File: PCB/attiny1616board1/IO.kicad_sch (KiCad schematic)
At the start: 41 parts, among them J10 SENSOR3_IN, J11 WS2813_OUT, J12 SERVO_OUT, J13 UPDI, J14 SERIAL, J15 SOLENOID1, J16 SOLENOID2, J8 SENSOR1_IN, J9 SENSOR2_IN, Q1 S8050, Q2 S8550, Q3 AO3400A, Q4 S8050, Q5 S8550, Q6 AO3400A, SW1 SENSOR1_TEST, SW2 SENSOR2_TEST, SW3 SENSOR3_TEST, SW4 SW_DIP_x08

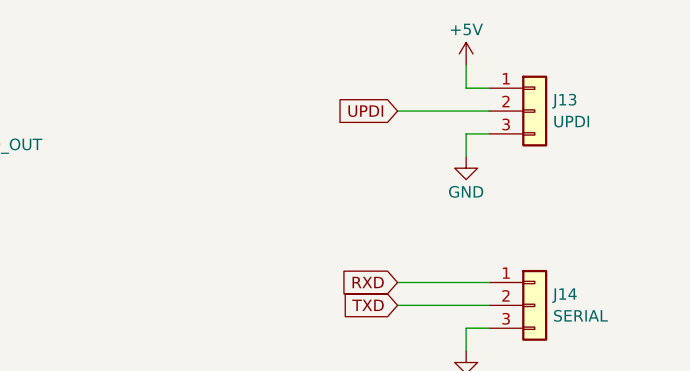
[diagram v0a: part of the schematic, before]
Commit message: 新7セグ・タイマー制御基板のデータを追加
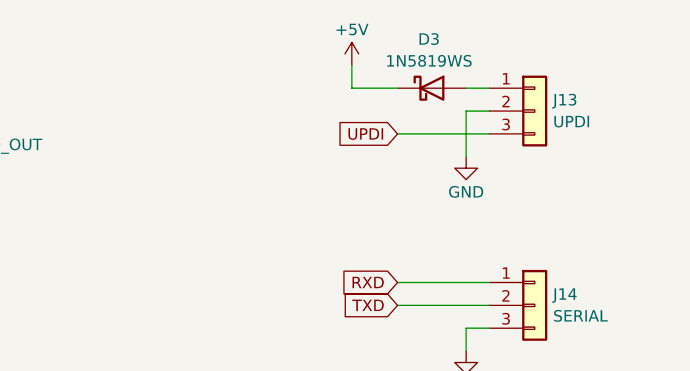
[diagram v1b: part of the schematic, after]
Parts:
- added D3: 1N5819WS, Diode_SMD:D_SOD-323, symbol Device:D_Schottky
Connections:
- net +5V: now also D3.1 (K); no longer J13.1 (Pin_1)
- net GND: now also J13.2 (Pin_2); no longer J13.3 (Pin_3)
- net UPDI: now also J13.3 (Pin_3); no longer J13.2 (Pin_2)
- new net: D3.2 (A), J13.1 (Pin_1)
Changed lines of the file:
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@@
     (stroke (width 0) (type default))
   )
-  (wire (pts (xy 251.46 30.48) (xy 251.46 33.02))
+  (wire (pts (xy 251.46 27.94) (xy 251.46 33.02))
     (stroke (width 0) (type default))
   )
@@
     (stroke (width 0) (type default))
   )
+  (wire (pts (xy 243.84 30.48) (xy 254 30.48))
+    (stroke (width 0) (type default))
+  )
   (wire (pts (xy 162.56 102.87) (xy 165.1 102.87))
     (stroke (width 0) (type default))
@@
     (stroke (width 0) (type default))
   )
-  (wire (pts (xy 254 30.48) (xy 251.46 30.48))
+  (wire (pts (xy 254 27.94) (xy 251.46 27.94))
     (stroke (width 0) (type default))
   )
@@
     (stroke (width 0) (type default))
   )
+  (wire (pts (xy 238.76 25.4) (xy 243.84 25.4))
+    (stroke (width 0) (type default))
+  )
   (wire (pts (xy 100.33 166.37) (xy 85.09 166.37))
     (stroke (width 0) (type default))
@@
     (stroke (width 0) (type default))
   )
-  (wire (pts (xy 251.46 25.4) (xy 251.46 22.86))
+  (wire (pts (xy 238.76 25.4) (xy 238.76 22.86))
     (stroke (width 0) (type default))
   )
@@
   )
   (wire (pts (xy 74.93 172.72) (xy 77.47 172.72))
-    (stroke (width 0) (type default))
-  )
-  (wire (pts (xy 243.84 27.94) (xy 254 27.94))
     (stroke (width 0) (type default))
   )
@@
     )
   )
-  (global_label "UPDI" (shape input) (at 243.84 27.94 180) (fields_autoplaced)
+  (global_label "UPDI" (shape input) (at 243.84 30.48 180) (fields_autoplaced)
     (effects (font (size 1.27 1.27)) (justify right))
-    (property "Intersheetrefs" "${INTERSHEET_REFS}" (at 236.3795 27.94 0)
+    (property "Intersheetrefs" "${INTERSHEET_REFS}" (at 236.3795 30.48 0)
       (effects (font (size 1.27 1.27)) (justify right) hide)
     )
@@
     )
   )
+  (symbol (lib_id "Device:D_Schottky") (at 247.65 25.4 0) (unit 1)
+    (in_bom yes) (on_board yes) (dnp no)
+    (property "Reference" "D3" (at 247.3325 19.9857 0)
+      (effects (font (size 1.27 1.27)))
+    )
+    (property "Value" "1N5819WS" (at 247.3325 22.4099 0)
+      (effects (font (size 1.27 1.27)))
+    )
+    (property "Footprint" "Diode_SMD:D_SOD-323" (at 247.65 25.4 0)
+      (effects (font (size 1.27 1.27)) hide)
+    )
+    (property "Datasheet" "~" (at 247.65 25.4 0)
+      (effects (font (size 1.27 1.27)) hide)
+    )
+    (property "LCSC" "C191023" (at 247.65 25.4 0)
+      (effects (font (size 1.27 1.27)) hide)
+    )
+    (pin "2")
+    (pin "1")
+    (instances
+      (project "attiny1616board1"
+        (path "/96ba6829-8a3e-4d81-9a4b-1c1c29c6350f/7613d6ae-36c0-4a05-b2dd-82f4e8851848"
+          (reference "D3") (unit 1)
+        )
+      )
+    )
+  )
   (symbol (lib_id "power:GND") (at 110.49 50.8 0) (unit 1)
     (in_bom yes) (on_board yes) (dnp no) (fields_autoplaced)
@@
     )
   )
-  (symbol (lib_id "power:+5V") (at 251.46 22.86 0) (unit 1)
-    (in_bom yes) (on_board yes) (dnp no)
-    (property "Reference" "#PWR031" (at 251.46 26.67 0)
-      (effects (font (size 1.27 1.27)) hide)
-    )
-    (property "Value" "+5V" (at 251.46 18.915 0)
-      (effects (font (size 1.27 1.27)))
-    )
-    (property "Footprint" "" (at 251.46 22.86 0)
-      (effects (font (size 1.27 1.27)) hide)
-    )
-    (property "Datasheet" "" (at 251.46 22.86 0)
-      (effects (font (size 1.27 1.27)) hide)
-    )
+  (symbol (lib_id "power:+5V") (at 238.76 22.86 0) (unit 1)
+    (in_bom yes) (on_board yes) (dnp no)
+    (property "Reference" "#PWR031" (at 238.76 26.67 0)
+      (effects (font (size 1.27 1.27)) hide)
+    )
+    (property "Value" "+5V" (at 238.76 18.915 0)
+      (effects (font (size 1.27 1.27)))
+    )
+    (property "Footprint" "" (at 238.76 22.86 0)
+      (effects (font (size 1.27 1.27)) hide)
+    )
+    (property "Datasheet" "" (at 238.76 22.86 0)
+      (effects (font (size 1.27 1.27)) hide)
+    )
